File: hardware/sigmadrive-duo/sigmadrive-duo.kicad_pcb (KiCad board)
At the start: 4 copper layers, 85 x 100 mm, 213 parts, among them J1 CONN_02X02, J2 CONN_02X05, J3 Conn_02x03_Odd_Even, J4 CONN_02X02, J5 Conn_02x03_Odd_Even, J6 629_105_150_921, M1 Conn_01x03, M1_SW1 CONN_02X02, M1_SW2 CONN_02X02, M2 Conn_01x03, M2_SW1 CONN_02X02, M2_SW2 CONN_02X02, Q1 NTMFS5C628NLT1G, Q10 NTMFS5C628NLT1G, Q11 NTMFS5C628NLT1G, Q12 NTMFS5C628NLT1G, Q2 NTMFS5C628NLT1G, Q3 NTMFS5C628NLT1G, Q4 NTMFS5C628NLT1G, Q5 NTMFS5C628NLT1G, Q6 NTMFS5C628NLT1G, Q7 NTMFS5C628NLT1G, Q8 NTMFS5C628NLT1G, Q9 NTMFS5C628NLT1G, SW2 SW_DIP_x04, U1 DRV8323RS, U12 SN65HVD75DGKR, U2 DRV8323RS, U3 SN65HVD75DGKR, U4 TPD4S009, U5 STM32F745VGTx, U6 TPD4S009, U7 TPS70933, U8 SN65HVD75DGKR, Y1 NX3225SA-12.000M-STD-CSR-1

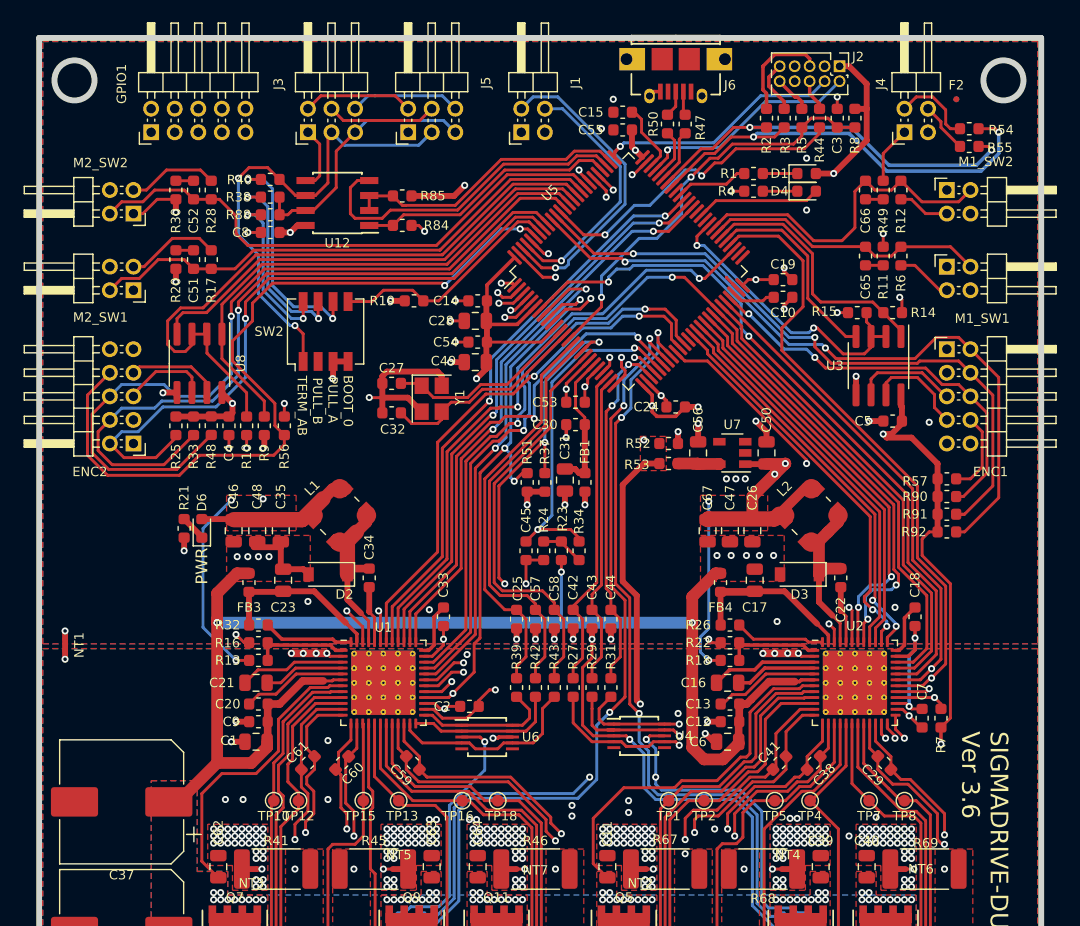
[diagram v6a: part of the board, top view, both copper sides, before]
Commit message: Hardware version 3.8. Adde support for external battery.
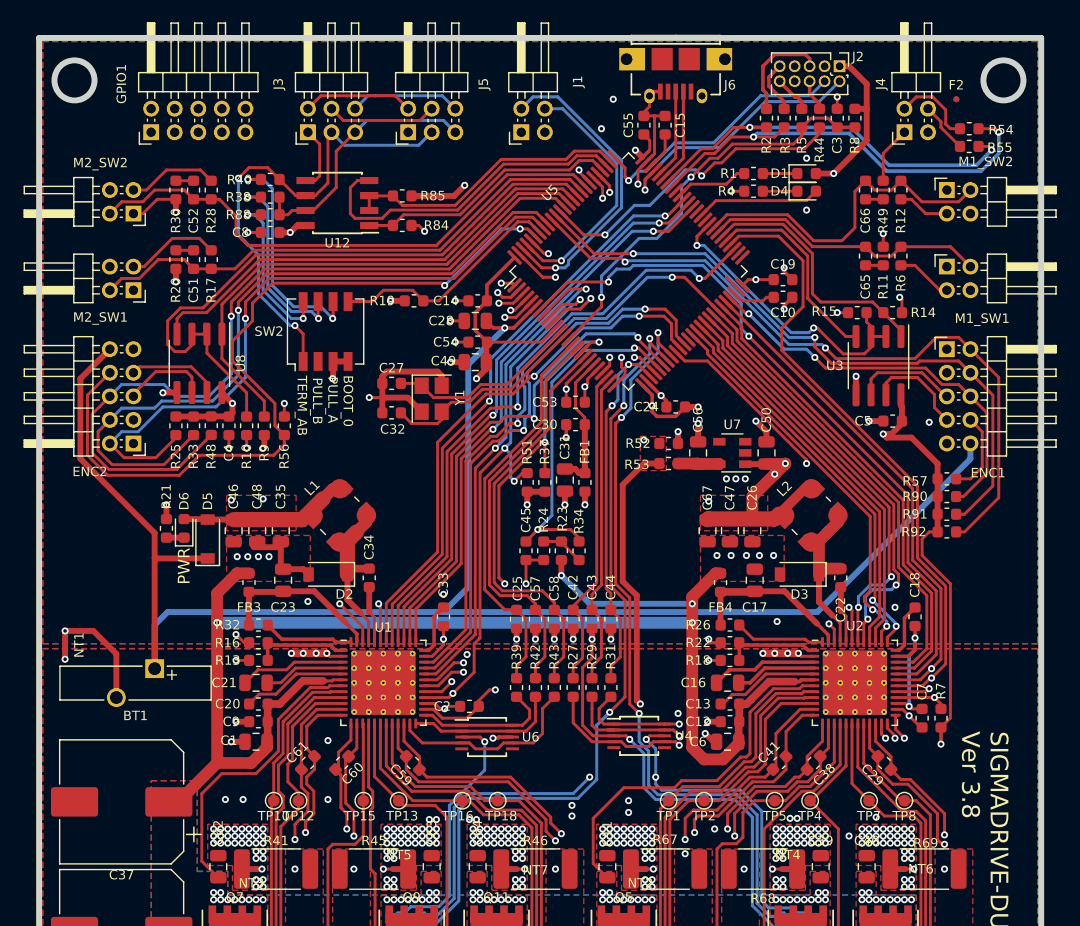
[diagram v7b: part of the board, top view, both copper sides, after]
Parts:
- removed R47, R50: 21, Resistor_SMD:R_0603_1608Metric
- added BT1: Battery_Cell, Battery:Battery_Panasonic_CR1220-VCN_Vertical_CircularHoles, F.Cu at (72.7, 114.7)
- added D5: STPS0560Z, Diode_SMD:D_SOD-123, F.Cu at (77.2, 103.7)
- moved C15 3.76 mm to (116.0, 68.6), turned to 270 degrees
- moved C55 1.84 mm to (114.2, 68.6), turned to 270 degrees
- moved D6 1.50 mm to (75.2, 102.8)
- moved R21 1.50 mm to (73.7, 102.8), turned to 270 degrees
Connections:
- C28 pad 1: +3V3 -> +BATT
- ENC1 pad 10: Net-(ENC1-Pad10) -> +BATT
- ENC1 pad 3: Net-(ENC1-Pad3) -> GND
- ENC2 pad 10: Net-(ENC2-Pad10) -> +BATT
- ENC2 pad 3: Net-(ENC2-Pad3) -> GND
- J6 pad 2: Net-(J6-Pad2) -> /MCU/PA11
- J6 pad 3: Net-(J6-Pad3) -> /MCU/PA12
- U5 pad 6: +3V3 -> +BATT
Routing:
- net +BATT: track 0.00 -> 146.8 mm, vias 0 -> 1
- net GND: track 203.2 -> 222.0 mm
- net VIN: track 172.1 -> 180.1 mm, vias 112 -> 113
- net /MCU/PA13: track 19.1 -> 22.9 mm
- net /MCU/PA11: track 4.58 -> 8.05 mm
- net /MCU/PA12: track 4.24 -> 7.57 mm
- net Net-(C15-Pad2): track 6.00 -> 3.15 mm
- net Net-(J6-Pad3): track 2.25 -> 0.00 mm
- net Net-(J6-Pad2): track 2.02 -> 0.00 mm
- net +3V3: track 417.3 -> 415.3 mm
- net /MCU/PA14: track 20.8 -> 22.6 mm
- net Net-(D6-Pad1): track 2.20 -> 1.50 mm
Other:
- board text added: "SIGMADRIVE-DUO Ver 3.8"
- board text removed: "SIGMADRIVE-DUO Ver 3.6"

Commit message: Hardware version 3.8. Adde support for external battery.
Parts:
- moved F2 37.0 mm to (145.1, 103.1)
- moved F4 37.0 mm to (145.1, 103.1)
